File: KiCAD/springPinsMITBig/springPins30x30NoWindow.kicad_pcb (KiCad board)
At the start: 2 copper layers, 30.5 x 30.5 mm, 22 parts, among them J1 CONN_02X06, J2 CONN_02X06

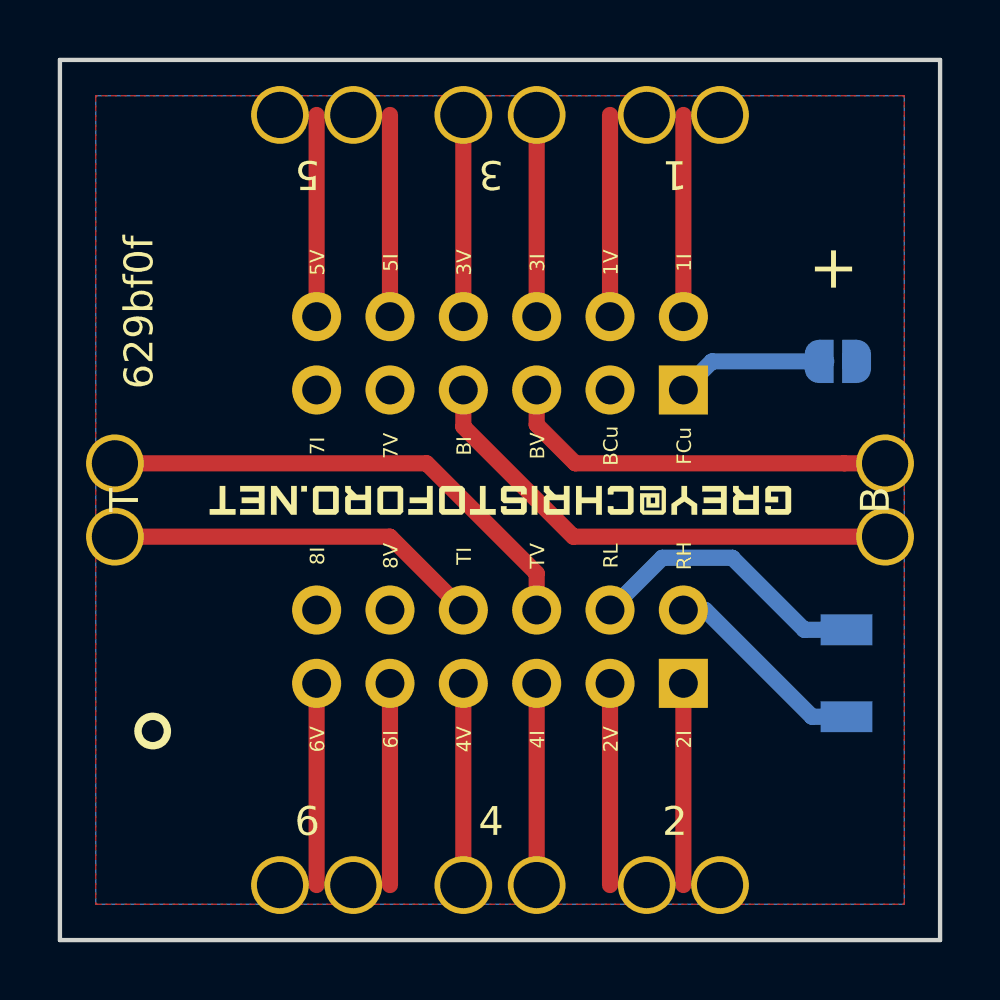
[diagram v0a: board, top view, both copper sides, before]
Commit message: adapter and photodiode board for mit
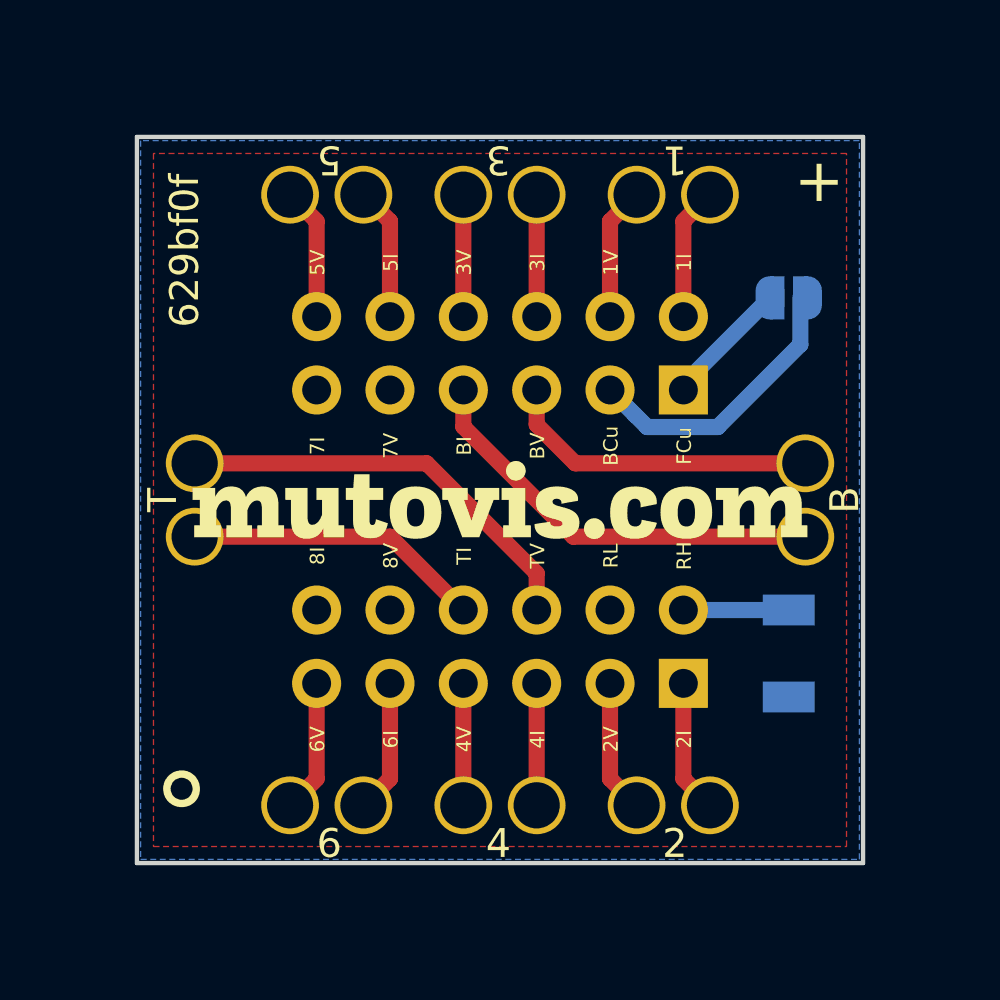
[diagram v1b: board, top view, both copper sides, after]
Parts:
- removed the L1 at (0.00, 0.00) (x2)
- added L1: grey@mutovis.com, logo:text, F.Cu at (0.00, 0.00)
- moved TP15 2.78 mm to (-7.27, -10.6)
- moved TP20 2.78 mm to (7.27, -10.6)
- moved TP3 2.78 mm to (-7.27, 10.6)
- moved TP8 2.78 mm to (7.27, 10.6)
- moved TP16 2.78 mm to (-4.73, -10.6)
- moved TP19 2.78 mm to (4.73, -10.6)
- moved TP4 2.78 mm to (-4.73, 10.6)
- moved TP7 2.78 mm to (4.73, 10.6)
- moved JP1 2.78 mm to (10.0, -7.00)
- moved TP10 2.76 mm to (10.6, 1.27)
- moved TP11 2.76 mm to (-10.6, -1.27)
- moved TP12 2.76 mm to (10.6, -1.27)
- moved TP17 2.76 mm to (-1.27, -10.6)
- moved TP18 2.76 mm to (1.27, -10.6)
- moved TP5 2.76 mm to (-1.27, 10.6)
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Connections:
- J1 pad 4: /RL -> Net-(J1-Pad4)
- J2 pad 3: /BCu -> GND
- JP1 pad 1: /BCu -> GND
- R1 pad 1: /RL -> GND
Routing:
- net /RL: track 9.97 -> 0.00 mm
- net GND: track 0.00 -> 9.92 mm
- net /RH: track 7.18 -> 3.65 mm
- net /VB: track 13.8 -> 11.1 mm
- net /VT: track 17.5 -> 14.7 mm
- net /V4: track 6.99 -> 4.22 mm
- net /V3: track 6.99 -> 4.22 mm
- net /IT: track 13.1 -> 10.4 mm
- net /IB: track 17.5 -> 14.7 mm
- net /I4: track 6.99 -> 4.22 mm
- net /I3: track 6.99 -> 4.22 mm
- net /V6: track 6.99 -> 4.60 mm
- net /V5: track 6.99 -> 4.60 mm
- net /V2: track 6.99 -> 4.60 mm
- net /V1: track 6.99 -> 4.60 mm
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- added copper zone on B.Cu, net GND
- removed copper zone on B.Cu, net /BCu
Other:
- board size 30.5 x 30.5 mm -> 25.1 x 25.1 mm

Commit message: update silk
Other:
- board text added: "8694043"
- board text removed: "629bf0f"
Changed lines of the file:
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@@
   )
   (setup
-    (last_trace_width 0.56)
+    (last_trace_width 0.25)
     (user_trace_width 0.2)
     (user_trace_width 0.56)
@@
       (usegerberextensions true)
       (usegerberattributes true)
-      (usegerberadvancedattributes true)
+      (usegerberadvancedattributes false)
       (creategerberjobfile false)
       (excludeedgelayer true)
@@
       (plotinvisibletext false)
       (padsonsilk false)
-      (subtractmaskfromsilk false)
+      (subtractmaskfromsilk true)
       (outputformat 1)
       (mirror false)
@@
     (effects (font (size 1 1) (thickness 0.25)))
   )
-  (gr_text 629bf0f (at -10.922 -8.636 90) (layer F.SilkS)
+  (gr_text 8694043 (at -10.922 -8.636 90) (layer F.SilkS)
     (effects (font (size 1 1) (thickness 0.175)))
   )
